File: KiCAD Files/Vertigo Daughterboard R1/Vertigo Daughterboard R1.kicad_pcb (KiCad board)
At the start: 4 copper layers, 33.5 x 27.2 mm, 27 parts, among them IC1 ICM-20602, IC2 DPS310XTSA1, J1 Conn_01x08_Pin, U1 NEO-6M-GPS, U2 24AA32A-I_MS

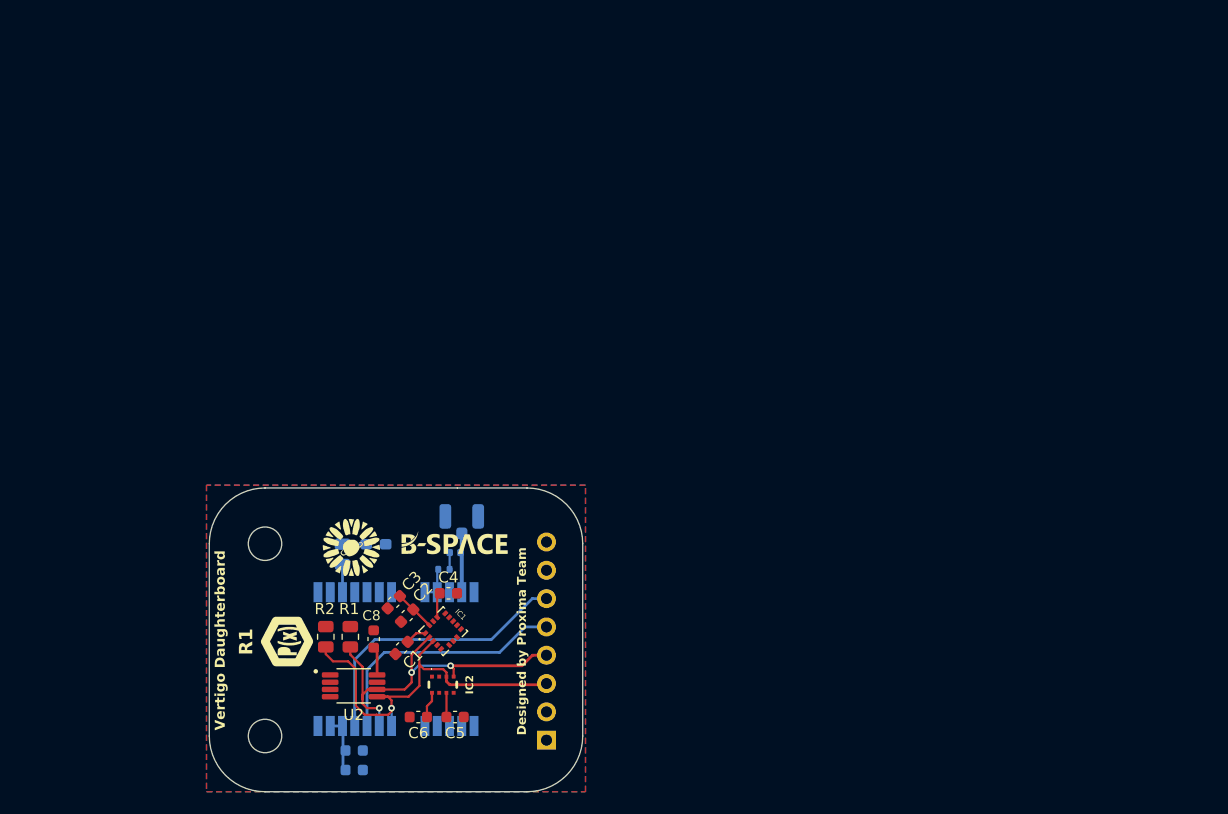
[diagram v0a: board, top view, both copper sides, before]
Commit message: switched I2C to SPI, new PCB shape, fix for BOM
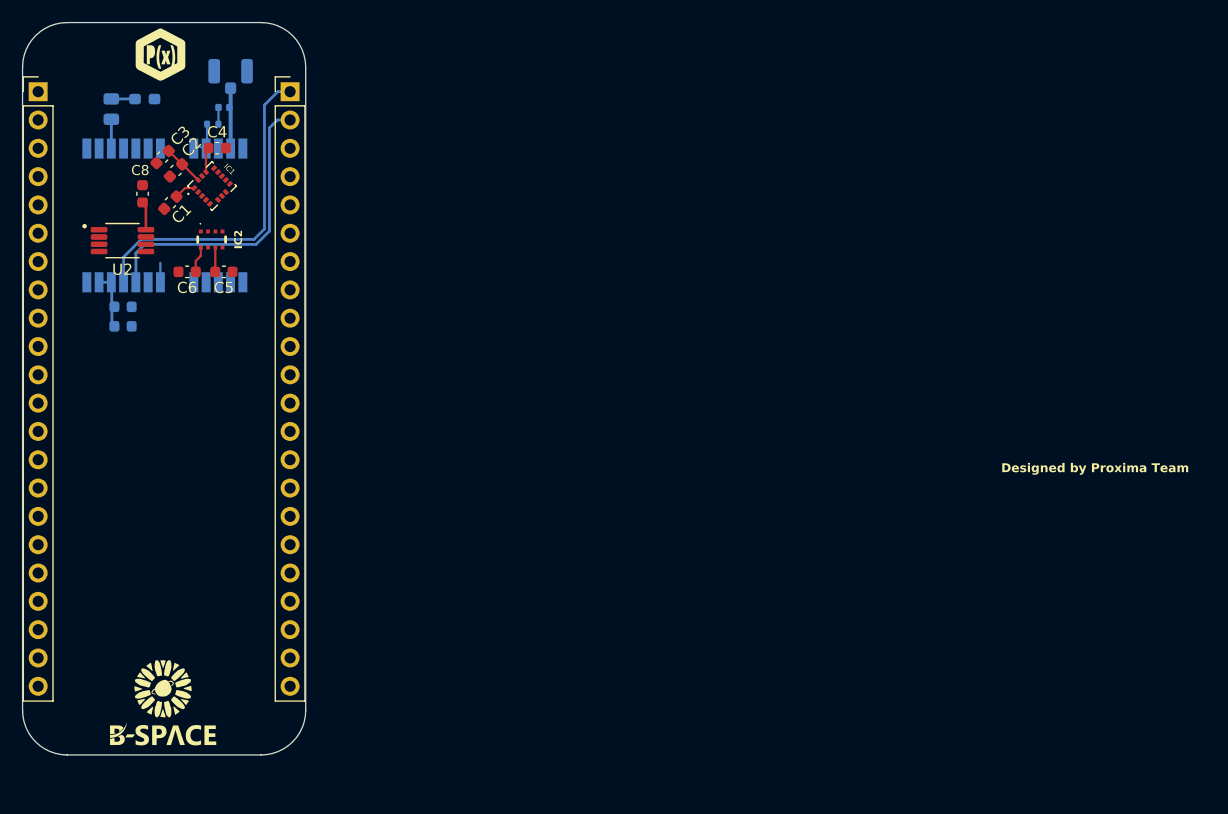
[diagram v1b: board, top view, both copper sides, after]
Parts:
- removed R1, R2: 10K, Resistor_SMD:R_0805_2012Metric
- removed the REF** at (121.8, 102.5)
- removed the REF** at (121.8, 85.2)
- added G***: LOGO, Vertigo Pro KiCad Libraries:b-space_logo_long, B.Cu at (112.6, 88.6)
- added G***: LOGO, Vertigo Pro KiCad Libraries:flower_space_logo, B.Cu at (112.5, 93.1)
- added J2: Conn_01x22_Socket, Connector_PinHeader_2.54mm:PinHeader_1x22_P2.54mm_Vertical, F.Cu at (124.0, 44.7)
- J1: value Conn_01x08_Pin -> Conn_01x22_Socket; footprint Connector_PinHeader_2.54mm:PinHeader_1x08_P2.54mm_Vertical -> Connector_PinHeader_2.54mm:PinHeader_1x22_P2.54mm_Vertical; moved to F.Cu
- moved J1 73.9 mm to (101.4, 44.7)
- moved G*** 53.8 mm to (112.4, 41.4), turned to 0 degrees
- moved C3 45.0 mm to (112.6, 50.6)
- moved U2 45.0 mm to (109.0, 58.1)
- moved C1 45.0 mm to (113.3, 54.7)
- moved C4 45.0 mm to (117.5, 49.8)
- moved R3 45.0 mm to (108.0, 46.3)
- moved R4 45.0 mm to (117.1, 47.6)
- moved AE1 45.0 mm to (118.7, 43.3)
- moved C5 45.0 mm to (118.1, 60.9)
- moved C8 45.0 mm to (110.8, 53.9)
- moved IC2 45.0 mm to (117.0, 58.0)
- moved L1 45.0 mm to (118.1, 46.1)
- moved C2 45.0 mm to (113.8, 51.8)
- moved IC1 45.0 mm to (117.0, 53.2)
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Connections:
- IC1 pad 2: /SCL -> /SCLK
- IC1 pad 3: /SDA -> /ESP_SDO
- IC1 pad 4: GND -> /ESP_SDI
- IC1 pad 5: unconnected-(IC1-CS-Pad5) -> +3.3V
- IC2 pad 2: unconnected-(IC2-CSB-Pad2) -> +3.3V
- IC2 pad 3: /SDA -> /ESP_SDO
- IC2 pad 4: /SCL -> /SCLK
- IC2 pad 5: unconnected-(IC2-SDO-Pad5) -> /ESP_SDI
- J1 pad 1: GND -> +3.3V
- J1 pad 2: +3.3V -> unconnected-(J1-Pin_2-Pad2)
- J1 pad 3: /SDA -> unconnected-(J1-Pin_3-Pad3)
- J1 pad 4: /SCL -> unconnected-(J1-Pin_4-Pad4)
- J1 pad 5: /UART_RX -> unconnected-(J1-Pin_5-Pad5)
- J1 pad 6: /UART_TX -> unconnected-(J1-Pin_6-Pad6)
- U1 pad 18: /SDA -> unconnected-(U1-SDA2-Pad18)
- U1 pad 19: /SCL -> unconnected-(U1-SCL2-Pad19)
- U2 pad 5: /SDA -> unconnected-(U2-SDA-Pad5)
- U2 pad 6: /SCL -> unconnected-(U2-SCL-Pad6)
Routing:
- net /SDA: track 36.3 -> 0.00 mm, vias 1 -> 0
- net /SCL: track 32.6 -> 0.00 mm, vias 3 -> 0
- net /UART_TX: track 25.4 -> 29.7 mm
- net /UART_RX: track 22.7 -> 26.7 mm
- net unconnected-(U1-SDA2-Pad18): track 0.00 -> 1.60 mm
- removed copper zone on B.Cu, net GND
- removed copper zone on F.Cu, net GND
- removed copper zone on In1.Cu, net GND
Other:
- board size 33.5 x 27.2 mm -> 25.4 x 65.7 mm
